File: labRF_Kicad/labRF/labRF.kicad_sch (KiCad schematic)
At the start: 1 part, among them U1 ATmega328-P

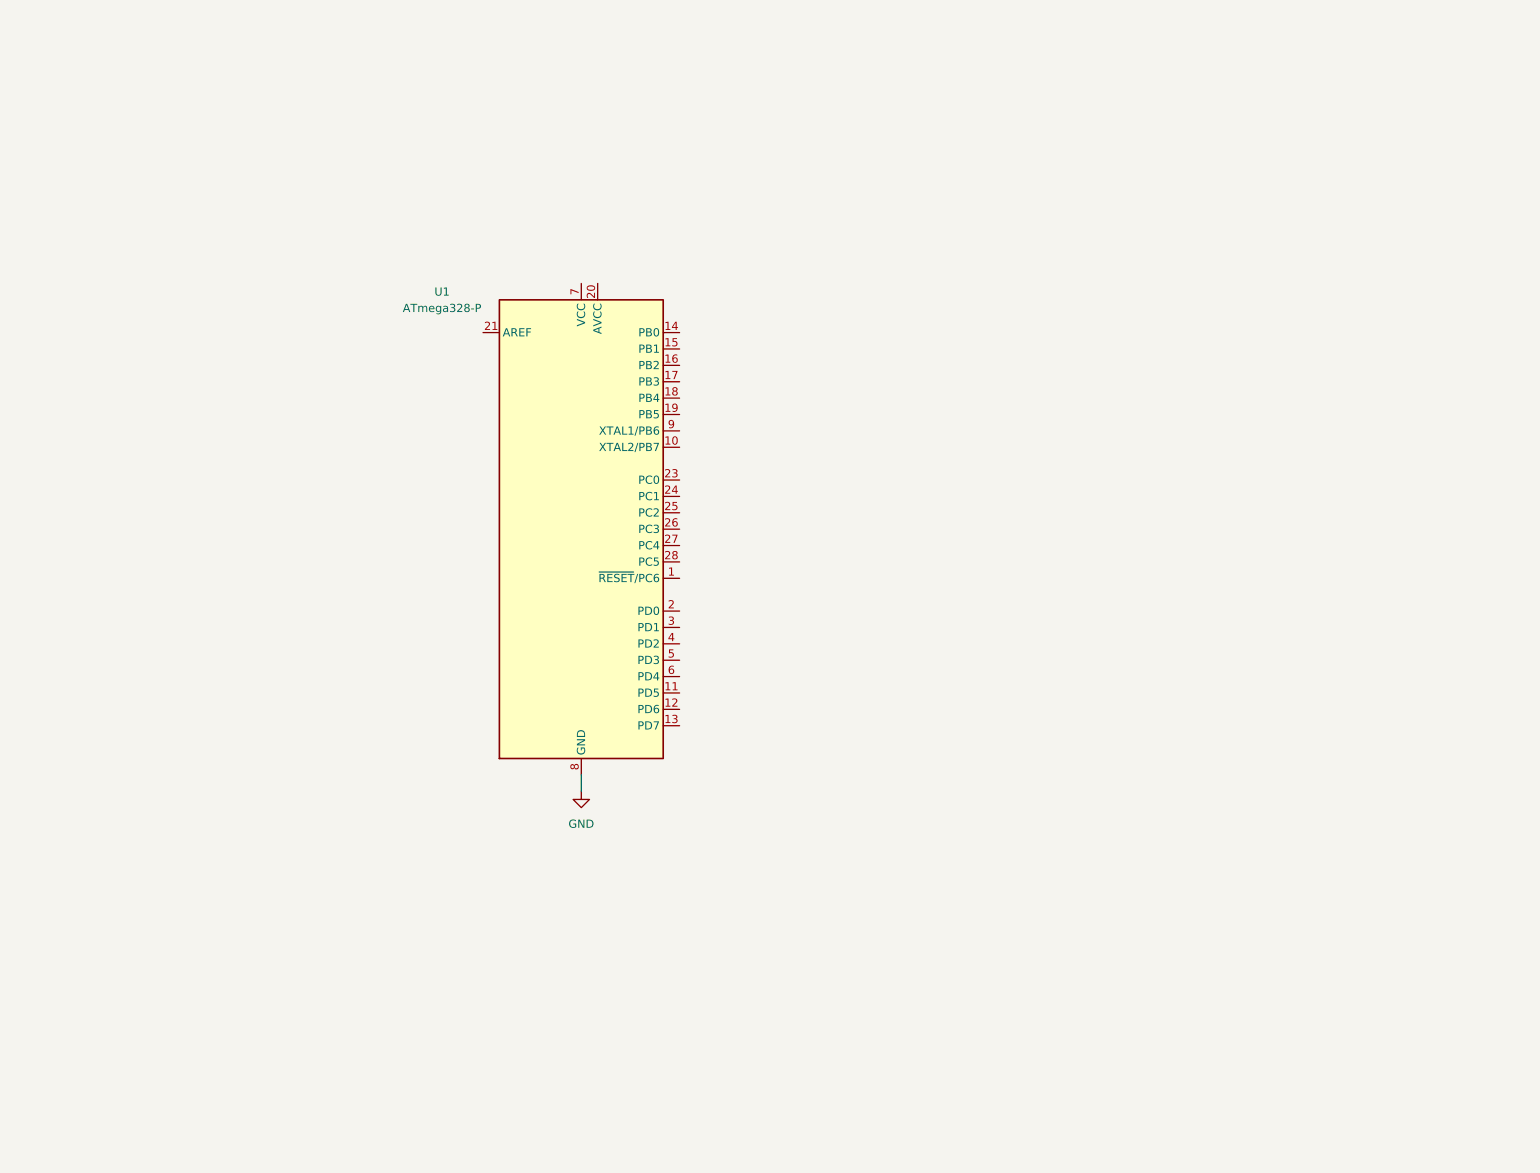
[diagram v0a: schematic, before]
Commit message: 328p schematics added
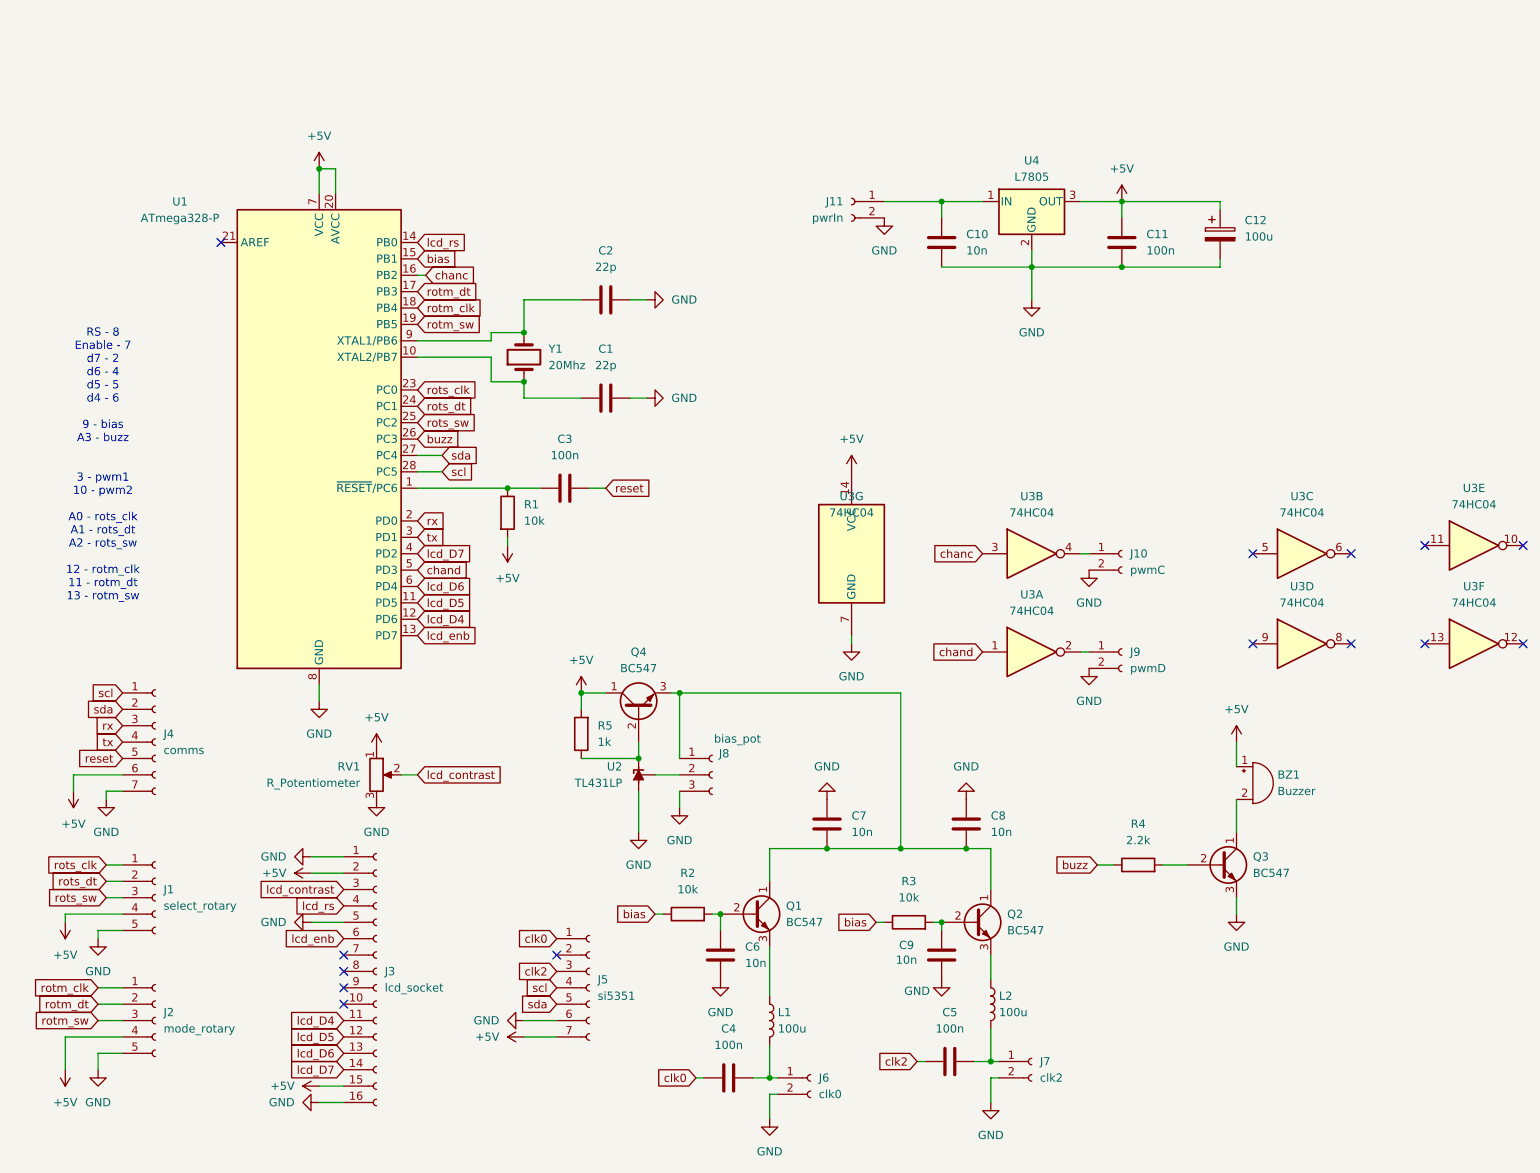
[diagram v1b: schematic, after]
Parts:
- added BZ1: Buzzer, symbol Device:Buzzer
- added C1, C2: 22p, symbol Device:C
- added C10, C6, C7, C8, C9: 10n, symbol Device:C
- added C11, C3, C4, C5: 100n, symbol Device:C
- added C12: 100u, symbol Device:C_Polarized
- added J1: select_rotary, symbol Connector:Conn_01x05_Socket
- added J10: pwmC, symbol Connector:Conn_01x02_Socket
- added J11: pwrIn, symbol Connector:Conn_01x02_Socket
- added J2: mode_rotary, symbol Connector:Conn_01x05_Socket
- added J3: lcd_socket, symbol Connector:Conn_01x16_Socket
- added J4: comms, symbol Connector:Conn_01x07_Socket
- added J5: si5351, symbol Connector:Conn_01x07_Socket
- added J6: clk0, symbol Connector:Conn_01x02_Socket
- added J7: clk2, symbol Connector:Conn_01x02_Socket
- added J8: bias_pot, symbol Connector:Conn_01x03_Socket
- added J9: pwmD, symbol Connector:Conn_01x02_Socket
- added L1, L2: 100u, symbol Device:L
- added Q1, Q2, Q3, Q4: BC547, Package_TO_SOT_THT:TO-92_Inline, symbol Transistor_BJT:BC547
- added R1, R2, R3: 10k, symbol Device:R
- added R4: 2.2k, symbol Device:R
- added R5: 1k, symbol Device:R
- added RV1: R_Potentiometer, symbol Device:R_Potentiometer
- added U2: TL431LP, Package_TO_SOT_THT:TO-92_Inline, symbol Reference_Voltage:TL431LP
- added U3: 74HC04, symbol 74xx:74HC04
- added U4: L7805, symbol Regulator_Linear:L7805
- added Y1: 20Mhz, symbol Device:Crystal
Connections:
- net GND: now also C1.2, C10.1, C11.1, C12.2, C2.2, C6.2, C7.1, C8.1, C9.2, J1.5 (Pin_5), J10.2 (Pin_2), J11.2 (Pin_2), J2.5 (Pin_5), J3.1 (Pin_1), J3.16 (Pin_16), J3.5 (Pin_5), J4.7 (Pin_7), J5.6 (Pin_6), J6.2 (Pin_2), J7.2 (Pin_2), J8.3 (Pin_3), J9.2 (Pin_2), Q3.3 (E), RV1.3, U2.2 (A), U3.7 (GND), U4.2 (GND)
- net at U1.1 (~{RESET}/PC6): now also C3.1, R1.1
- net at U1.10 (XTAL2/PB7): now also C1.1, Y1.1
- net lcd_D5: now reaches U1.11 (PD5)
- net lcd_D5: now also J3.12 (Pin_12)
- net lcd_D4: now reaches U1.12 (PD6)
- net lcd_D4: now also J3.11 (Pin_11)
- net lcd_enb: now reaches U1.13 (PD7)
- net lcd_enb: now also J3.6 (Pin_6)
- net lcd_rs: now reaches U1.14 (PB0)
- net lcd_rs: now also J3.4 (Pin_4)
- net bias: now reaches U1.15 (PB1)
- net bias: now also R2.1, R3.1
- net chanc: now reaches U1.16 (PB2)
- net chanc: now also U3.3
- net rotm_dt: now reaches U1.17 (PB3)
- net rotm_dt: now also J2.2 (Pin_2)
- net rotm_clk: now reaches U1.18 (PB4)
- net rotm_clk: now also J2.1 (Pin_1)
- net rotm_sw: now reaches U1.19 (PB5)
- net rotm_sw: now also J2.3 (Pin_3)
- net rx: now reaches U1.2 (PD0)
- net rx: now also J4.3 (Pin_3)
- net +5V: now reaches U1.20 (AVCC)
- net +5V: now also U1.7 (VCC), BZ1.1 (+), C11.2, C12.1, J1.4 (Pin_4), J2.4 (Pin_4), J3.15 (Pin_15), J3.2 (Pin_2), J4.6 (Pin_6), J5.7 (Pin_7), Q4.1 (C), R1.2, R5.2, RV1.1, U3.14 (VCC), U4.3 (OUT)
- net rots_clk: now reaches U1.23 (PC0)
- net rots_clk: now also J1.1 (Pin_1)
- net rots_dt: now reaches U1.24 (PC1)
- net rots_dt: now also J1.2 (Pin_2)
- net rots_sw: now reaches U1.25 (PC2)
- net rots_sw: now also J1.3 (Pin_3)
- net buzz: now reaches U1.26 (PC3)
- net buzz: now also R4.1
- net sda: now reaches U1.27 (PC4)
- net sda: now also J4.2 (Pin_2), J5.5 (Pin_5)
- net scl: now reaches U1.28 (PC5)
- net scl: now also J4.1 (Pin_1), J5.4 (Pin_4)
- net tx: now reaches U1.3 (PD1)
- net tx: now also J4.4 (Pin_4)
- net lcd_D7: now reaches U1.4 (PD2)
- net lcd_D7: now also J3.14 (Pin_14)
- net chand: now reaches U1.5 (PD3)
- net chand: now also U3.1
- net lcd_D6: now reaches U1.6 (PD4)
- net lcd_D6: now also J3.13 (Pin_13)
- net at U1.9 (XTAL1/PB6): now also C2.1, Y1.2
- new net: C7.2, C8.2, J8.1 (Pin_1), Q1.1 (C), Q2.1 (C), Q4.3 (E)
- new net: C5.2, J7.1 (Pin_1), L2.2
- new net: C4.2, J6.1 (Pin_1), L1.2
- new net: C10.2, J11.1 (Pin_1), U4.1 (IN)
- new net: Q4.2 (B), R5.1, U2.3 (K)
- new net: J10.1 (Pin_1), U3.4
- new net: Q3.2 (B), R4.2
- new net: L2.1, Q2.3 (E)
- new net: BZ1.2 (-), Q3.1 (C)
- new net: C9.1, Q2.2 (B), R3.2
- new net: C6.1, Q1.2 (B), R2.2
- new net: L1.1, Q1.3 (E)
- new net: J9.1 (Pin_1), U3.2
- new net: J8.2 (Pin_2), U2.1 (REF)
- new net clk0: C4.1, J5.1 (Pin_1)
- new net clk2: C5.1, J5.3 (Pin_3)
- new net lcd_contrast: J3.3 (Pin_3), RV1.2
- new net reset: C3.2, J4.5 (Pin_5)
- no-connect marks 0 -> 14
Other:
- note added: "RS - 8 Enable - 7 d7 - 2 d6 - 4 d5 - 5 d4 - 6 9 - bias A3 - buzz 3 - pwm1 10 - pwm2 A0 - rots_clk A1 - rots_dt A2 - rots_sw 12 - rotm_clk 11 - rotm_dt 13 - rotm_sw"
- moved on the sheet: U1

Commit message: Finieshed PCB Design
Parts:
- added C13: 100n, Capacitor_THT:C_Disc_D5.0mm_W2.5mm_P2.50mm, symbol Device:C
- added C14: 100u, Capacitor_THT:CP_Radial_D8.0mm_P5.00mm, symbol Device:C_Polarized
- added JP1, JP2: Jumper_2_Open, Connector_PinHeader_2.54mm:PinHeader_1x02_P2.54mm_Vertical, symbol Jumper:Jumper_2_Open
- BZ1: footprint (none) -> Buzzer_Beeper:Buzzer_D14mm_H7mm_P10mm
- C1, C10, C11, C2, C3, C4, C5, C6, C7, C8, C9: footprint (none) -> Capacitor_THT:C_Disc_D5.0mm_W2.5mm_P2.50mm
- C12: footprint (none) -> Capacitor_THT:CP_Radial_D8.0mm_P5.00mm
- J1, J2: footprint (none) -> Connector_PinHeader_2.54mm:PinHeader_1x05_P2.54mm_Vertical
- J10, J11, J6, J7, J9: footprint (none) -> Connector_PinHeader_2.54mm:PinHeader_1x02_P2.54mm_Vertical
- J3: footprint (none) -> Connector_PinHeader_2.54mm:PinHeader_1x16_P2.54mm_Vertical
- J4, J5: footprint (none) -> Connector_PinHeader_2.54mm:PinHeader_1x07_P2.54mm_Vertical
- J8: footprint (none) -> Connector:FanPinHeader_1x03_P2.54mm_Vertical
- L1, L2: footprint (none) -> Inductor_THT:L_Toroid_Vertical_L14.7mm_W8.6mm_P5.58mm_Pulse_KM-1
- R1, R2, R3, R4, R5: footprint (none) -> Resistor_THT:R_Axial_DIN0207_L6.3mm_D2.5mm_P10.16mm_Horizontal
- RV1: footprint (none) -> Potentiometer_THT:Potentiometer_Bourns_3386P_Vertical
- U3: footprint (none) -> Package_DIP:DIP-14_W7.62mm
- U4: footprint (none) -> Package_TO_SOT_THT:TO-220-3_Vertical
- Y1: footprint (none) -> Crystal:Crystal_HC49-U_Vertical
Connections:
- net GND: now also C13.1, C14.2
- net at C7.2, C8.2, J8.1 (Pin_1)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: now also C13.2, C14.1
- net at C5.2, J7.1 (Pin_1): now also JP2.1 (A); no longer L2.2
- net at C4.2, J6.1 (Pin_1): now also JP1.1 (A); no longer L1.2
- new net: JP2.2 (B), L2.2
- new net: JP1.2 (B), L1.2
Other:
- moved on the sheet: BZ1, C1, C10, C11, C12, C2, C3, C4, C5, C6, C7, C8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
